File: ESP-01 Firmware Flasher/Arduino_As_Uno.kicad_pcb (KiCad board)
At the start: 2 copper layers, 68.6 x 53.3 mm, 15 parts, among them J1 CONN_01X02, J2 CONN_01X02, P1 Power, P2 Analog, P3 Digital, P4 Digital, P5 CONN_01X01, P6 CONN_01X01, P7 CONN_01X01, P8 CONN_01X01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

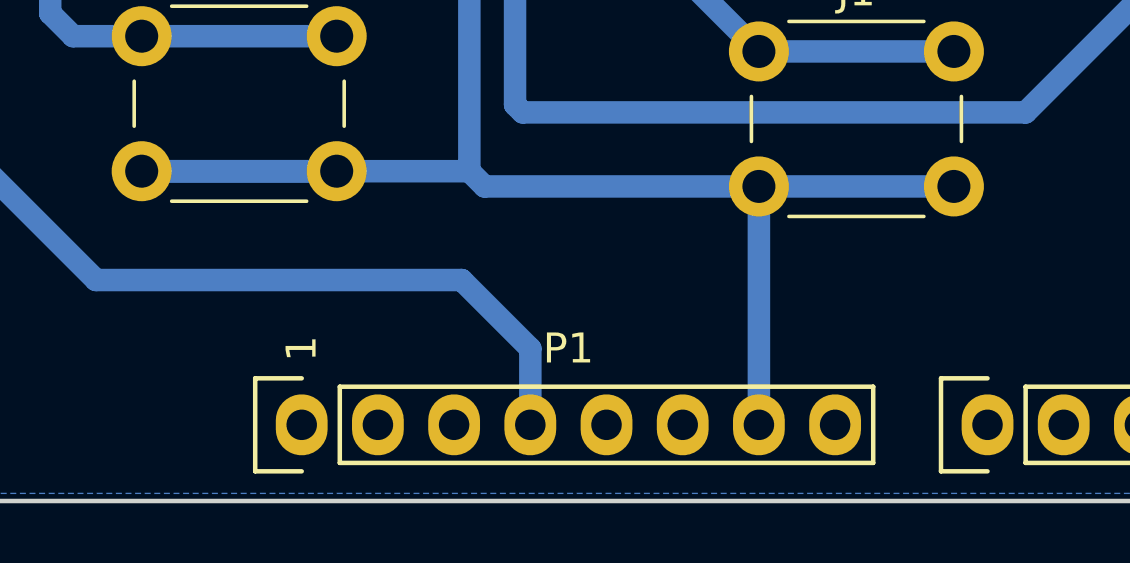
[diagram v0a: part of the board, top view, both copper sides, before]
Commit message: Update ESP-01 Board
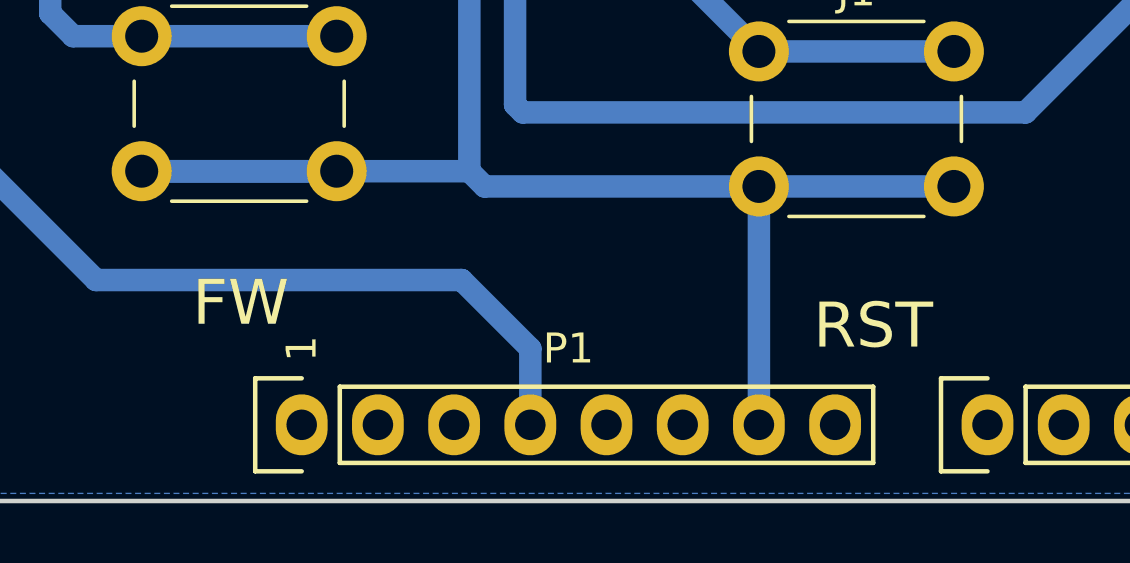
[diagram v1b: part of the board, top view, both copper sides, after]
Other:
- board text added: "FW"
- board text added: "RST"
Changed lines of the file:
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@@
     (links 23)
     (no_connects 2)
-    (area 104.572999 71.542 182.071334 127.694)
+    (area 110.922999 72.949999 179.653001 126.440001)
     (thickness 1.6)
-    (drawings 27)
+    (drawings 29)
     (tracks 61)
     (zones 0)
@@
     (0 F.Cu signal)
     (31 B.Cu signal)
+    (37 F.SilkS user)
     (44 Edge.Cuts user)
   )
   (setup
-    (last_trace_width 0.75)
+    (last_trace_width 0.25)
     (user_trace_width 0.5)
     (user_trace_width 0.75)
@@
       (net 9 "Net-(R4-Pad2)"))
   )
+  (gr_text FW (at 136.906 119.761) (layer F.SilkS)
+    (effects (font (size 1.5 1.5) (thickness 0.3)))
+  )
+  (gr_text RST (at 157.988 120.523) (layer F.SilkS)
+    (effects (font (size 1.5 1.5) (thickness 0.3)))
+  )
   (gr_text 1 (at 138.938 121.285 90) (layer F.SilkS)
